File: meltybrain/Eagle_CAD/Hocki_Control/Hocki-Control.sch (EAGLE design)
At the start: 96 parts, among them J1 JST-SR_5, P1 B5B-PH-K, P2 B5B-PH-K, P3 B2B-PH-K, U1 TEENSY_4.1, U10 TLV3502AIDCNR, U11 NL27WZ32USG, U12 NL27WZ32USG, U13 HMC1052L-TR, U14 LMV358, U15 IRF7509, U16 TMUX1219DCKR, U17 LMV358, U18 LMV358, U2 ADXL375, U3 ADXL375, U4 ADXL375, U5 ADXL375, U6 LMH6612MAX/NOPB, U7 LMH6612MAX/NOPB, U8 LMH6612MAX/NOPB, U9 LMH6612MAX/NOPB

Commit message: started control power
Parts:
- removed P1, P2: B5B-PH-K, con-jst-ph:B5B-PH-K
- removed P3: B2B-PH-K, con-jst-ph:B2B-PH-K
- added C38: 0.1u, rcl:C-USC0603
- added C39, C40: 1u, rcl:C-USC0603
- added J2: SM05B-SRSS-TB(LF)(SN), Hocki_Library:SM05B-SRSS-TB(LF)(SN)
- added U19: TLV73310PDBVT, Hocki_Library:TLV73310PDBVT
- J1: value JST-SR_5 -> SM05B-SRSS-TB(LF)(SN); device Hocki_Library:JST-SR_5 -> Hocki_Library:SM05B-SRSS-TB(LF)(SN)
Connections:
- new net +3V3: C30.1, C32.1, C33.1, C40.1, R28.1, R34.1, U13.VB, U14.VCC+, U18.VCC+, U19.OUT
- new net N$5: C31.1, U17.VCC+
- net 3.3V: now also C38.1, U1.3.3V; no longer C30.1, C31.1, C32.1, C33.1, R28.1, R34.1, U13.VB, U14.VCC+, U17.VCC+, U18.VCC+
- net 5V: now also C39.1, U19.EN, U19.IN
- net GND: now also C38.2, C39.2, C40.2, U19.GND
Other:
- moved on the sheet: C17

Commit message: added IR connectors
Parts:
- added C41: 1u, rcl:C-USC0603
- added C42, C43: 100p, rcl:C-USC0603
- added C44: 2.2u, rcl:C-USC0603
- added U20: AP2210K-5.0TRG1, Hocki_Library:AP2210K-5.0TRG1
- C40: value 1u -> 2.2u
- U19: value TLV73310PDBVT -> AP2210K-3.3TRG1; device Hocki_Library:TLV73310PDBVT -> Hocki_Library:AP2210K-3.3TRG1
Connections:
- removed net N$5: C31.1, U17.VCC+
- new net 9V: C41.1, J1.1, J1.SHIELD, J2.1, J2.SHIELD, U20.EN, U20.IN
- new net IR_BOTTOM_A0: J2.3, U1.35/TX8
- new net IR_BOTTOM_A1: J2.4, U1.34/RX8
- new net IR_TOP_A0: J1.3, U1.37/PWM/CS
- new net IR_TOP_A1: J1.4, U1.36/PWM/CS
- new net N$11: C43.1, U19.BYP
- new net N$8: C42.1, U20.BYP
- net +3V3: now also C31.1, U17.VCC+
- net 5V: now also C44.1, U20.OUT
- net GND: now also C41.2, C42.2, C43.2, C44.2, J1.5, J2.5, U20.GND
- net IR_BOTTOM: now also J2.2
- net IR_SEL: now also U1.33/PWM/MCLK2; no longer U1.36/PWM/CS
- net IR_TOP: now also J1.2
- net S/R: now also U1.32/OUT1B; no longer U1.33/PWM/MCLK2
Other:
- moved on the sheet: C39, C40

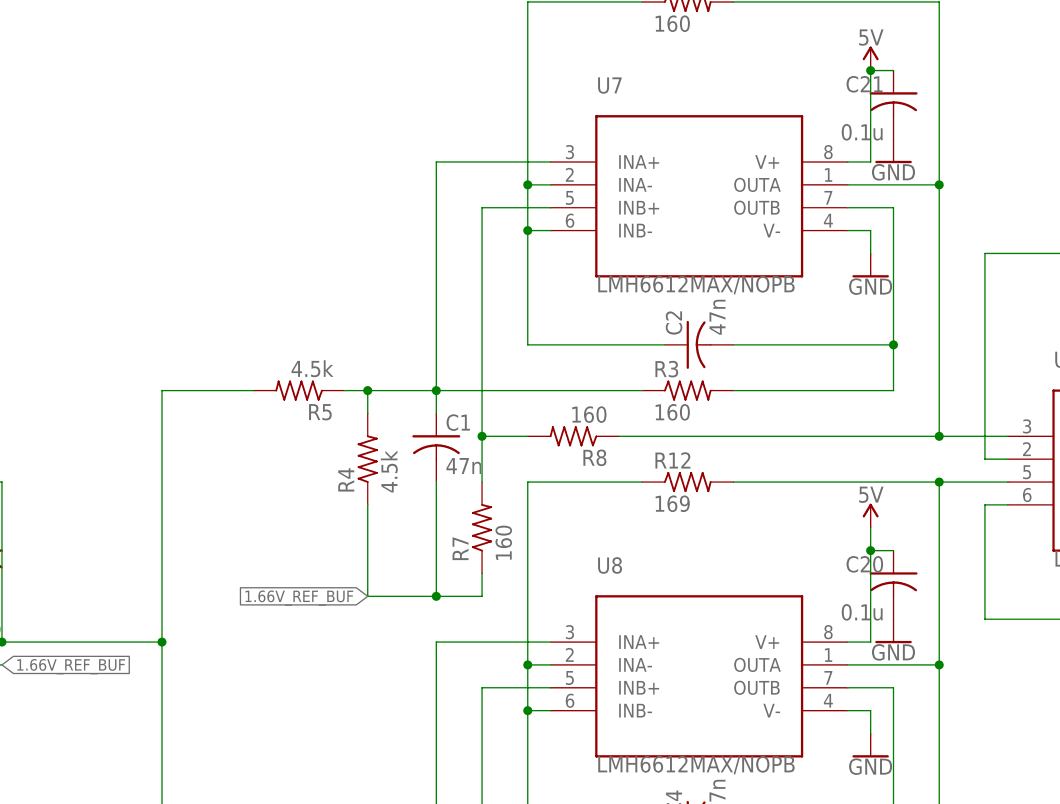
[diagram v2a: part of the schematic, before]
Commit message: fixed 10k bandpass
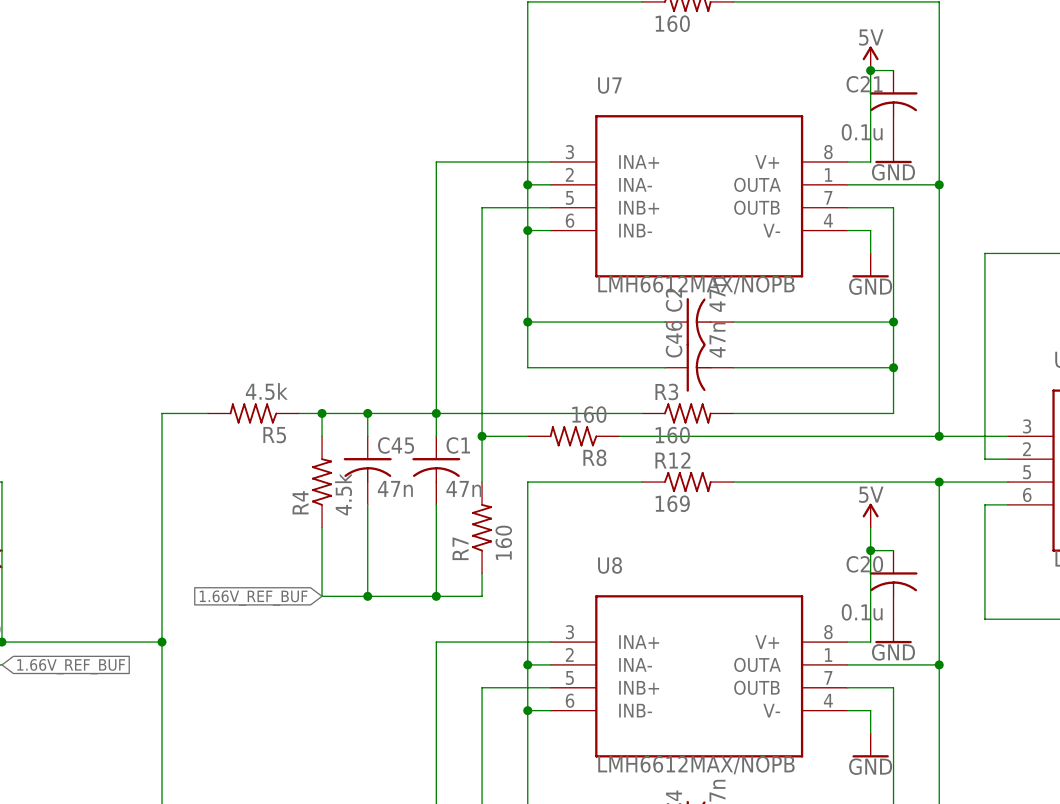
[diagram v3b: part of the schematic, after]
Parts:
- added C45, C46: 47n, rcl:C-USC1206
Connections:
- net 1.66V_REF_BUF: now also C45.2
- net 10K_FB: now also C46.2
- net 10K_IN: now also C45.1
- net N$4: now also C46.1
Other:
- moved on the sheet: C1, C2, R3, R4, R5
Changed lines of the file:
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@@
 <part name="SUPPLY19" library="Hocki_Library" deviceset="9V" device=""/>
 <part name="SUPPLY20" library="Hocki_Library" deviceset="9V" device=""/>
+<part name="C45" library="rcl" library_urn="urn:adsk.eagle:library:334" deviceset="C-US" device="C1206" package3d_urn="urn:adsk.eagle:package:23618/2" value="47n"/>
+<part name="C46" library="rcl" library_urn="urn:adsk.eagle:library:334" deviceset="C-US" device="C1206" package3d_urn="urn:adsk.eagle:package:23618/2" value="47n"/>
 </parts>
 <sheets>
@@
 <attribute name="VALUE" x="154.94" y="248.666" size="1.778" layer="96" align="top-center"/>
 </instance>
-<instance part="R3" gate="G$1" x="238.76" y="287.02" smashed="yes">
-<attribute name="NAME" x="234.95" y="288.5186" size="1.778" layer="95"/>
-<attribute name="VALUE" x="234.95" y="283.718" size="1.778" layer="96"/>
-</instance>
-<instance part="R4" gate="G$1" x="203.2" y="279.4" smashed="yes" rot="R90">
-<attribute name="NAME" x="201.7014" y="275.59" size="1.778" layer="95" rot="R90"/>
-<attribute name="VALUE" x="206.502" y="275.59" size="1.778" layer="96" rot="R90"/>
-</instance>
-<instance part="R5" gate="G$1" x="195.58" y="287.02" smashed="yes" rot="R180">
-<attribute name="NAME" x="199.39" y="285.5214" size="1.778" layer="95" rot="R180"/>
-<attribute name="VALUE" x="199.39" y="290.322" size="1.778" layer="96" rot="R180"/>
+<instance part="R3" gate="G$1" x="238.76" y="284.48" smashed="yes">
+<attribute name="NAME" x="234.95" y="285.9786" size="1.778" layer="95"/>
+<attribute name="VALUE" x="234.95" y="281.178" size="1.778" layer="96"/>
+</instance>
+<instance part="R4" gate="G$1" x="198.12" y="276.86" smashed="yes" rot="R90">
+<attribute name="NAME" x="196.6214" y="273.05" size="1.778" layer="95" rot="R90"/>
+<attribute name="VALUE" x="201.422" y="273.05" size="1.778" layer="96" rot="R90"/>
+</instance>
+<instance part="R5" gate="G$1" x="190.5" y="284.48" smashed="yes" rot="R180">
+<attribute name="NAME" x="194.31" y="282.9814" size="1.778" layer="95" rot="R180"/>
+<attribute name="VALUE" x="194.31" y="287.782" size="1.778" layer="96" rot="R180"/>
 </instance>
 <instance part="GND7" gate="1" x="259.08" y="299.72" smashed="yes">
@@
 <attribute name="VALUE" x="309.88" y="299.974" size="1.778" layer="96" align="bottom-center"/>
 </instance>
-<instance part="C1" gate="G$1" x="210.82" y="281.94" smashed="yes">
-<attribute name="NAME" x="211.836" y="282.575" size="1.778" layer="95"/>
-<attribute name="VALUE" x="211.836" y="277.749" size="1.778" layer="96"/>
-</instance>
-<instance part="C2" gate="G$1" x="238.76" y="292.1" smashed="yes" rot="R90">
-<attribute name="NAME" x="238.125" y="293.116" size="1.778" layer="95" rot="R90"/>
-<attribute name="VALUE" x="242.951" y="293.116" size="1.778" layer="96" rot="R90"/>
+<instance part="C1" gate="G$1" x="210.82" y="279.4" smashed="yes">
+<attribute name="NAME" x="211.836" y="280.035" size="1.778" layer="95"/>
+<attribute name="VALUE" x="211.836" y="275.209" size="1.778" layer="96"/>
+</instance>
+<instance part="C2" gate="G$1" x="238.76" y="294.64" smashed="yes" rot="R90">
+<attribute name="NAME" x="238.125" y="295.656" size="1.778" layer="95" rot="R90"/>
+<attribute name="VALUE" x="242.951" y="295.656" size="1.778" layer="96" rot="R90"/>
 </instance>
 <instance part="C3" gate="G$1" x="210.82" y="228.6" smashed="yes">
@@
 <instance part="SUPPLY20" gate="G$1" x="-2.54" y="238.76" smashed="yes">
 <attribute name="VALUE" x="-2.54" y="241.554" size="1.778" layer="96" align="bottom-center"/>
+</instance>
+<instance part="C45" gate="G$1" x="203.2" y="279.4" smashed="yes">
+<attribute name="NAME" x="204.216" y="280.035" size="1.778" layer="95"/>
+<attribute name="VALUE" x="204.216" y="275.209" size="1.778" layer="96"/>
+</instance>
+<instance part="C46" gate="G$1" x="238.76" y="289.56" smashed="yes" rot="R90">
+<attribute name="NAME" x="238.125" y="290.576" size="1.778" layer="95" rot="R90"/>
+<attribute name="VALUE" x="242.951" y="290.576" size="1.778" layer="96" rot="R90"/>
 </instance>
 </instances>
@@
 <wire x1="162.56" y1="259.08" x2="180.34" y2="259.08" width="0.1524" layer="91"/>
 <junction x="162.56" y="259.08"/>
-<wire x1="180.34" y1="259.08" x2="180.34" y2="287.02" width="0.1524" layer="91"/>
+<wire x1="180.34" y1="259.08" x2="180.34" y2="284.48" width="0.1524" layer="91"/>
 <pinref part="R5" gate="G$1" pin="2"/>
-<wire x1="180.34" y1="287.02" x2="190.5" y2="287.02" width="0.1524" layer="91"/>
+<wire x1="180.34" y1="284.48" x2="185.42" y2="284.48" width="0.1524" layer="91"/>
 <wire x1="180.34" y1="259.08" x2="180.34" y2="233.68" width="0.1524" layer="91"/>
 <junction x="180.34" y="259.08"/>
@@
 <pinref part="U7" gate="A" pin="OUTB"/>
 <wire x1="256.54" y1="307.34" x2="261.62" y2="307.34" width="0.1524" layer="91"/>
-<wire x1="261.62" y1="307.34" x2="261.62" y2="292.1" width="0.1524" layer="91"/>
-<wire x1="261.62" y1="292.1" x2="243.84" y2="292.1" width="0.1524" layer="91"/>
+<wire x1="261.62" y1="307.34" x2="261.62" y2="294.64" width="0.1524" layer="91"/>
+<wire x1="261.62" y1="294.64" x2="243.84" y2="294.64" width="0.1524" layer="91"/>
 <pinref part="R3" gate="G$1" pin="2"/>
-<wire x1="243.84" y1="287.02" x2="261.62" y2="287.02" width="0.1524" layer="91"/>
-<wire x1="261.62" y1="287.02" x2="261.62" y2="292.1" width="0.1524" layer="91"/>
-<junction x="261.62" y="292.1"/>
+<wire x1="243.84" y1="284.48" x2="261.62" y2="284.48" width="0.1524" layer="91"/>
+<wire x1="261.62" y1="284.48" x2="261.62" y2="289.56" width="0.1524" layer="91"/>
+<junction x="261.62" y="294.64"/>
 <pinref part="C2" gate="G$1" pin="2"/>
+<pinref part="C46" gate="G$1" pin="2"/>
+<wire x1="261.62" y1="289.56" x2="261.62" y2="294.64" width="0.1524" layer="91"/>
+<wire x1="243.84" y1="289.56" x2="261.62" y2="289.56" width="0.1524" layer="91"/>
+<junction x="261.62" y="289.56"/>
 </segment>
 </net>
@@
 <pinref part="U7" gate="A" pin="INB-"/>
 <wire x1="223.52" y1="304.8" x2="220.98" y2="304.8" width="0.1524" layer="91"/>
-<wire x1="220.98" y1="304.8" x2="220.98" y2="292.1" width="0.1524" layer="91"/>
-<wire x1="220.98" y1="292.1" x2="236.22" y2="292.1" width="0.1524" layer="91"/>
+<wire x1="220.98" y1="304.8" x2="220.98" y2="294.64" width="0.1524" layer="91"/>
+<wire x1="220.98" y1="294.64" x2="236.22" y2="294.64" width="0.1524" layer="91"/>
 <pinref part="U7" gate="A" pin="INA-"/>
 <wire x1="223.52" y1="309.88" x2="220.98" y2="309.88" width="0.1524" layer="91"/>
@@
 <wire x1="220.98" y1="330.2" x2="233.68" y2="330.2" width="0.1524" layer="91"/>
 <pinref part="C2" gate="G$1" pin="1"/>
+<pinref part="C46" gate="G$1" pin="1"/>
+<wire x1="236.22" y1="289.56" x2="220.98" y2="289.56" width="0.1524" layer="91"/>
+<wire x1="220.98" y1="289.56" x2="220.98" y2="294.64" width="0.1524" layer="91"/>
+<junction x="220.98" y="294.64"/>
 </segment>
 </net>
@@
 <segment>
 <pinref part="R3" gate="G$1" pin="1"/>
-<wire x1="233.68" y1="287.02" x2="210.82" y2="287.02" width="0.1524" layer="91"/>
-<wire x1="210.82" y1="287.02" x2="210.82" y2="284.48" width="0.1524" layer="91"/>
+<wire x1="233.68" y1="284.48" x2="210.82" y2="284.48" width="0.1524" layer="91"/>
+<wire x1="210.82" y1="284.48" x2="210.82" y2="281.94" width="0.1524" layer="91"/>
 <pinref part="R4" gate="G$1" pin="2"/>
-<wire x1="203.2" y1="284.48" x2="203.2" y2="287.02" width="0.1524" layer="91"/>
-<wire x1="203.2" y1="287.02" x2="210.82" y2="287.02" width="0.1524" layer="91"/>
-<junction x="210.82" y="287.02"/>
+<wire x1="198.12" y1="281.94" x2="198.12" y2="284.48" width="0.1524" layer="91"/>
+<wire x1="198.12" y1="284.48" x2="203.2" y2="284.48" width="0.1524" layer="91"/>
+<junction x="210.82" y="284.48"/>
 <pinref part="R5" gate="G$1" pin="1"/>
-<wire x1="200.66" y1="287.02" x2="203.2" y2="287.02" width="0.1524" layer="91"/>
-<junction x="203.2" y="287.02"/>
+<wire x1="203.2" y1="284.48" x2="210.82" y2="284.48" width="0.1524" layer="91"/>
+<wire x1="195.58" y1="284.48" x2="198.12" y2="284.48" width="0.1524" layer="91"/>
+<junction x="198.12" y="284.48"/>
 <pinref part="U7" gate="A" pin="INA+"/>
 <wire x1="223.52" y1="312.42" x2="210.82" y2="312.42" width="0.1524" layer="91"/>
-<wire x1="210.82" y1="312.42" x2="210.82" y2="287.02" width="0.1524" layer="91"/>
+<wire x1="210.82" y1="312.42" x2="210.82" y2="284.48" width="0.1524" layer="91"/>
 <pinref part="C1" gate="G$1" pin="1"/>
+<pinref part="C45" gate="G$1" pin="1"/>
+<wire x1="203.2" y1="281.94" x2="203.2" y2="284.48" width="0.1524" layer="91"/>
+<junction x="203.2" y="284.48"/>
 </segment>
 </net>
@@
 <segment>
 <pinref part="R4" gate="G$1" pin="1"/>
-<wire x1="203.2" y1="274.32" x2="203.2" y2="264.16" width="0.1524" layer="91"/>
+<wire x1="198.12" y1="271.78" x2="198.12" y2="264.16" width="0.1524" layer="91"/>
+<wire x1="198.12" y1="264.16" x2="203.2" y2="264.16" width="0.1524" layer="91"/>
+<pinref part="R7" gate="G$1" pin="1"/>
 <wire x1="203.2" y1="264.16" x2="210.82" y2="264.16" width="0.1524" layer="91"/>
-<pinref part="R7" gate="G$1" pin="1"/>
 <wire x1="210.82" y1="264.16" x2="215.9" y2="264.16" width="0.1524" layer="91"/>
 <wire x1="215.9" y1="264.16" x2="215.9" y2="266.7" width="0.1524" layer="91"/>
-<wire x1="210.82" y1="276.86" x2="210.82" y2="264.16" width="0.1524" layer="91"/>
+<wire x1="210.82" y1="274.32" x2="210.82" y2="264.16" width="0.1524" layer="91"/>
 <junction x="210.82" y="264.16"/>
-<label x="203.2" y="264.16" size="1.27" layer="95" rot="R180" xref="yes"/>
+<label x="198.12" y="264.16" size="1.27" layer="95" rot="R180" xref="yes"/>
 <pinref part="C1" gate="G$1" pin="2"/>
-</segment>
-<segment>
+<pinref part="C45" gate="G$1" pin="2"/>
+<wire x1="203.2" y1="274.32" x2="203.2" y2="264.16" width="0.1524" layer="91"/>
+<junction x="203.2" y="264.16"/>
+</segment>
+<segment>

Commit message: forgot to save before pushing...
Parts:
- J1, J2: value SM05B-SRSS-TB(LF)(SN) -> SM03B-SRSS-TB(LF)(SN); device Hocki_Library:SM05B-SRSS-TB(LF)(SN) -> Hocki_Library:SM03B-SRSS-TB(LF)(SN)
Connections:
- removed net IR_BOTTOM_A0: J2.3, U1.35/TX8
- removed net IR_BOTTOM_A1: J2.4, U1.34/RX8
- removed net IR_TOP_A0: J1.3, U1.37/PWM/CS
- removed net IR_TOP_A1: J1.4, U1.36/PWM/CS
- net 5V: now also J1.SHIELD, J2.SHIELD
- net 9V: no longer J1.SHIELD, J2.SHIELD
- net GND: now also J1.3, J2.3; no longer J1.5, J2.5
- net IR_SEL: now also U1.37/PWM/CS; no longer U1.33/PWM/MCLK2

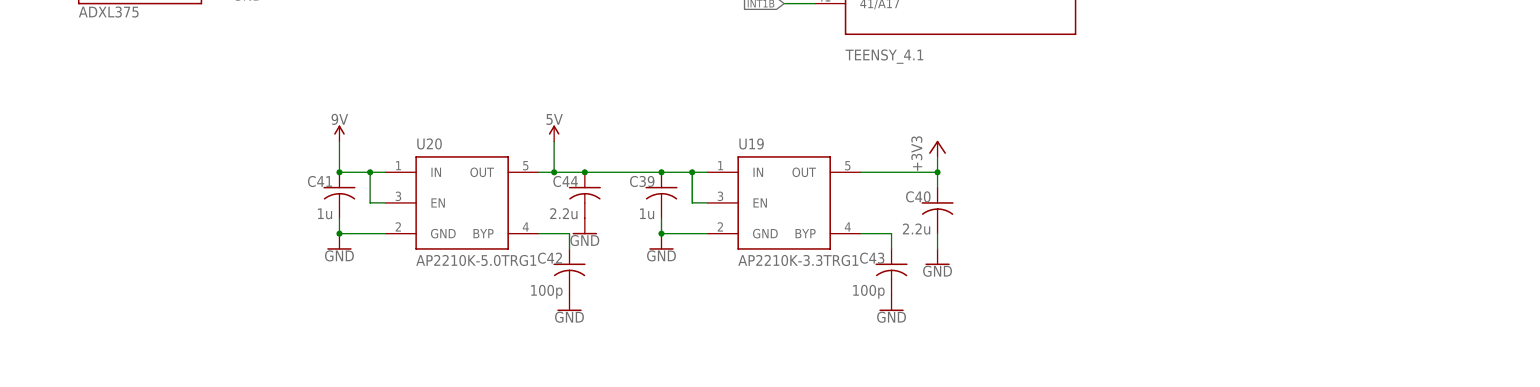
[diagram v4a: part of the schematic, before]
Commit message: power in
traces under capacitors be sketch...tried to avoid...
24-9 regulator is in
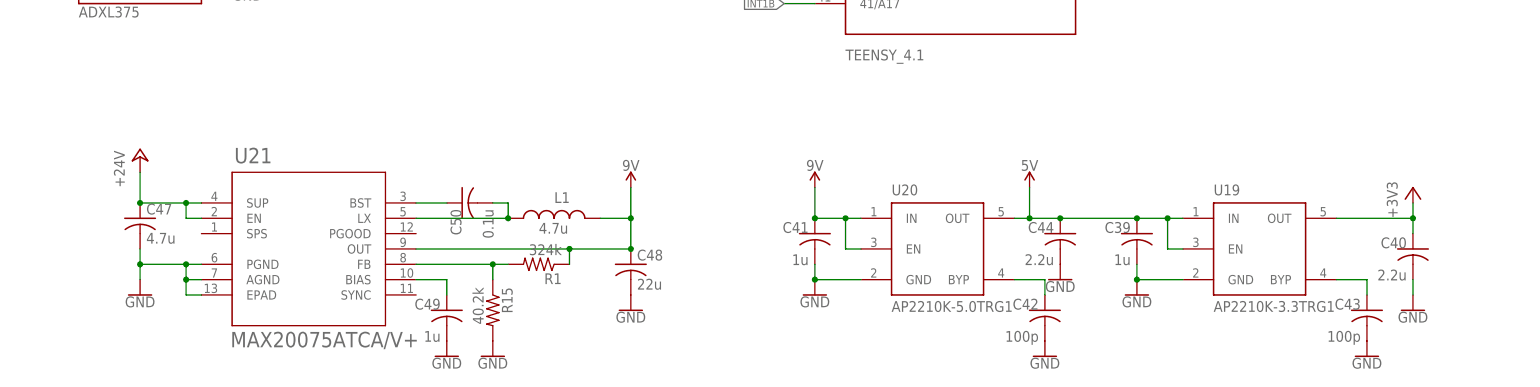
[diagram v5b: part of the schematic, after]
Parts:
- added C47: 4.7u, rcl:C-USC1206
- added C48: 22u, rcl:C-USC1206
- added C49: 1u, rcl:C-USC0603
- added C50: 0.1u, rcl:C-USC0603
- added L1: 4.7u, Hocki_Library:CBC2518T4R7M
- added R1: 324k, rcl:R-US_R0603
- added R15: 40.2k, rcl:R-US_R0603
- added U21: MAX20075ATCA/V+, Hocki_Library:MAX20075ATCA/V+
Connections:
- new net +24V: C47.1, U21.EN, U21.SUP
- new net N$1: C50.1, U21.BST
- new net N$12: R1.2, R15.1, U21.FB
- new net N$3: C50.2, L1.1, U21.LX
- new net N$6: C49.1, U21.BIAS
- net 9V: now also C48.1, L1.2, R1.1, U21.OUT
- net GND: now also C47.2, C48.2, C49.2, R15.2, U21.AGND, U21.EPAD, U21.PGND
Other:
- moved on the sheet: C39, C40, C41, C42, C43, C44, U19, U20
